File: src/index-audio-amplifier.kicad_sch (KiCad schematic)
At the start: 61 parts, among them J1 CU3616SASCLA004-LF, J2 SWD_PicoprobeCandybar, J3 Conn_01x02, J4 Conn_01x02, U1 RP2040, U2 RT6150B-33GQW, U3 W25Q16JVUXIQ, U4 MAX98360CENL, U5 TLV70033_SOT23-5, U6 MAX98360CENL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

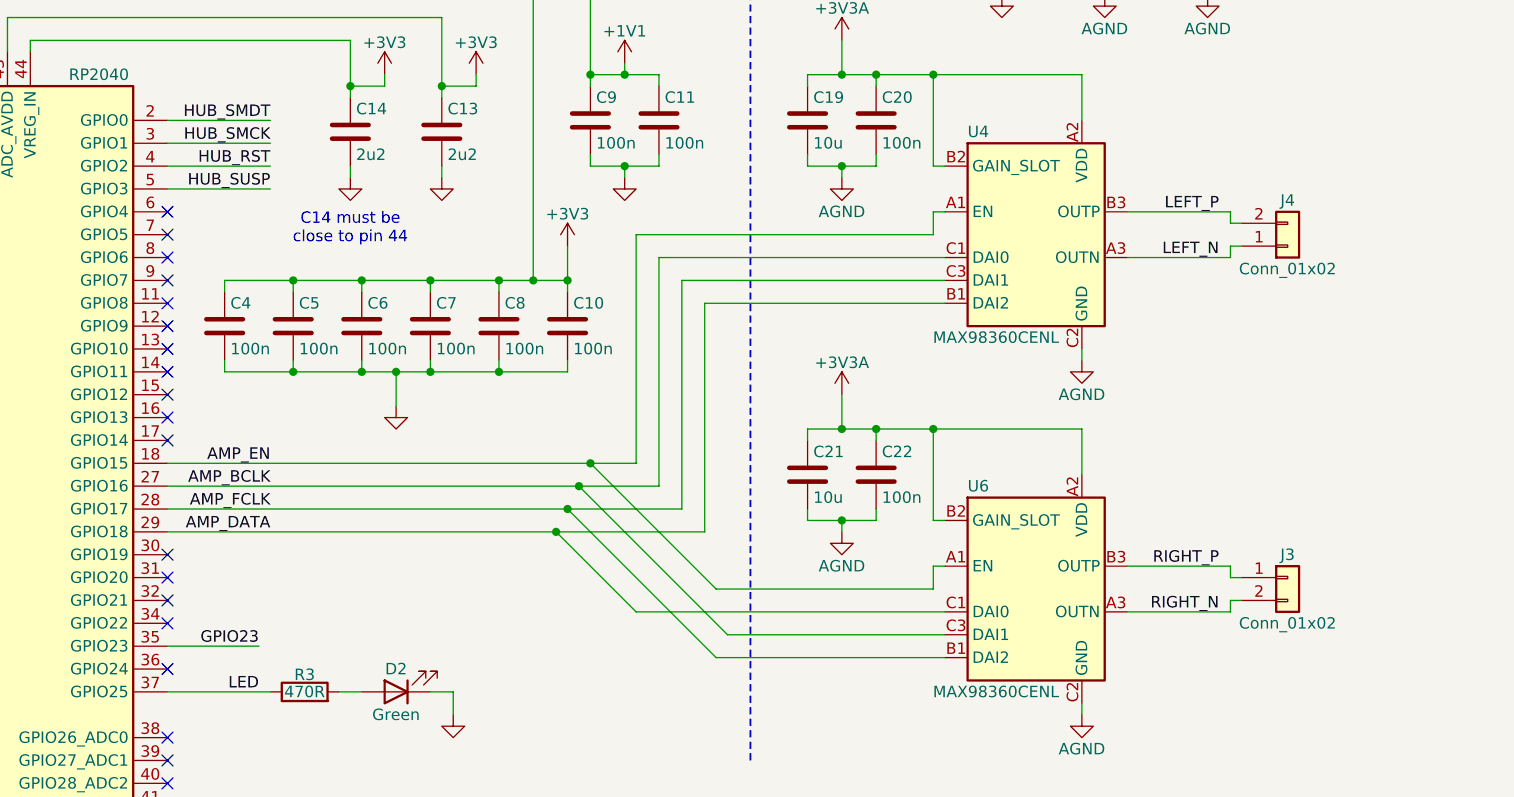
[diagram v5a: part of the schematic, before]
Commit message: Tie MAX98360 ENs to VDD to save on traces
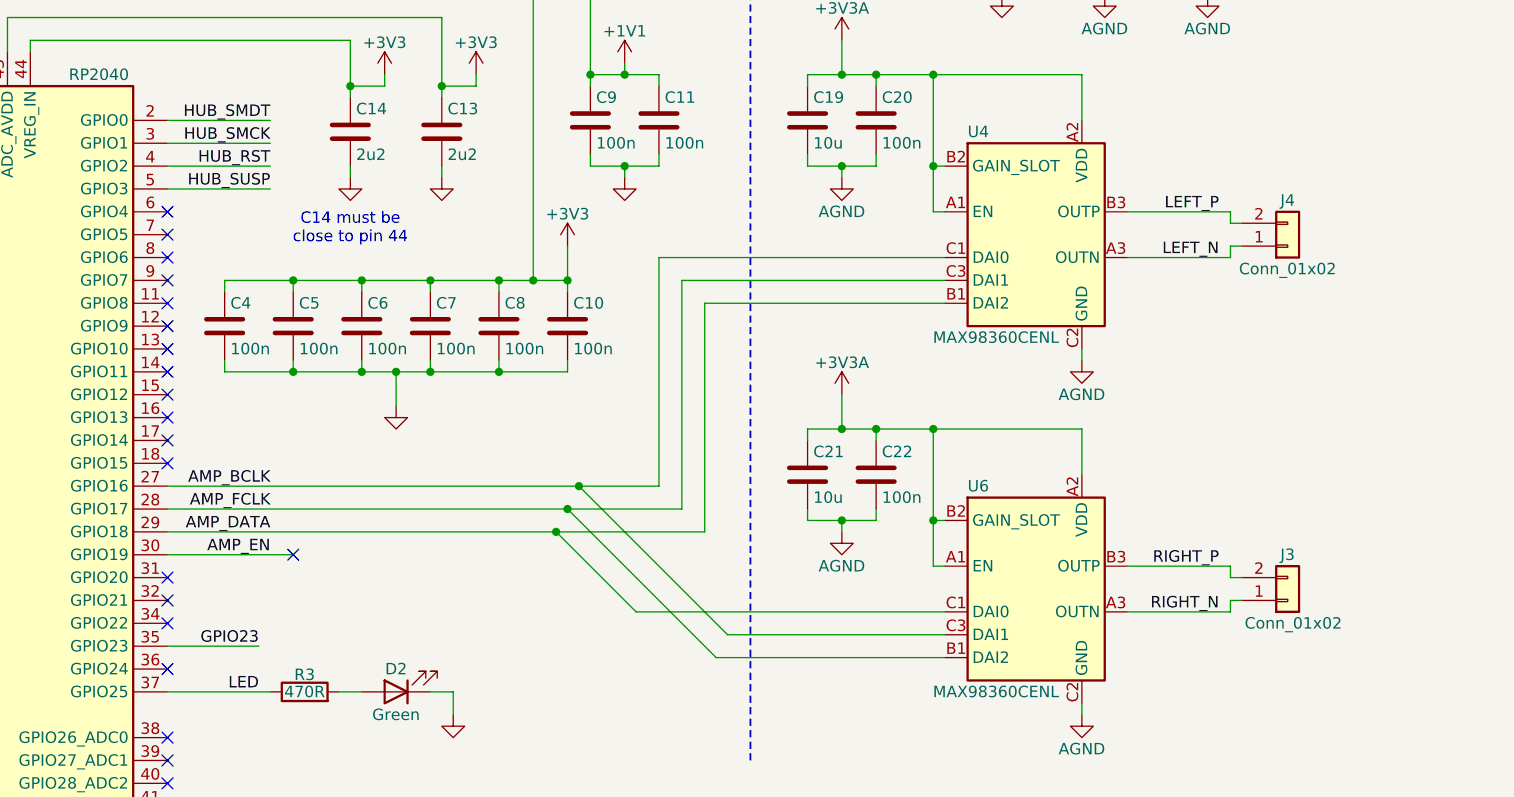
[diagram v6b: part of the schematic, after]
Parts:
- C19, C21: footprint Capacitor_SMD:C_0603_1608Metric -> Capacitor_SMD:C_0402_1005Metric
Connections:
- net +3V3A: now also U4.A1 (EN), U6.A1 (EN)
- net AMP_EN: now also U1.30 (GPIO19); no longer U1.18 (GPIO15), U4.A1 (EN), U6.A1 (EN)
- net RIGHT_N: now also J3.1 (Pin_1); no longer J3.2 (Pin_2)
- net RIGHT_P: now also J3.2 (Pin_2); no longer J3.1 (Pin_1)
- no-connect marks 31 -> 32
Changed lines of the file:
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@@
 	)
 	(junction
+		(at 236.22 151.13)
+		(diameter 0)
+		(color 0 0 0 0)
+	)
+	(junction
 		(at 35.56 90.17)
 		(diameter 0)
@@
 	)
 	(junction
-		(at 198.12 144.78)
-		(diameter 0)
-		(color 0 0 0 0)
-	)
-	(junction
 		(at 72.39 39.37)
 		(diameter 0)
@@
 	)
 	(junction
+		(at 236.22 111.76)
+		(diameter 0)
+		(color 0 0 0 0)
+	)
+	(junction
 		(at 97.79 25.4)
 		(diameter 0)
@@
 	)
 	(no_connect
+		(at 165.1 154.94)
+	)
+	(no_connect
 		(at 151.13 162.56)
 	)
@@
 	)
 	(no_connect
-		(at 151.13 154.94)
+		(at 151.13 144.78)
 	)
 	(no_connect
@@
 	(wire
 		(pts
-			(xy 203.2 119.38) (xy 236.22 119.38)
-		)
-		(stroke
-			(width 0)
-			(type default)
-		)
-	)
-	(wire
-		(pts
 			(xy 171.45 97.79) (xy 171.45 102.87)
 		)
@@
 	(wire
 		(pts
+			(xy 236.22 111.76) (xy 236.22 116.84)
+		)
+		(stroke
+			(width 0)
+			(type default)
+		)
+	)
+	(wire
+		(pts
 			(xy 107.95 25.4) (xy 97.79 25.4)
 		)
@@
 	(wire
 		(pts
-			(xy 236.22 158.75) (xy 236.22 156.21)
-		)
-		(stroke
-			(width 0)
-			(type default)
-		)
-	)
-	(wire
-		(pts
 			(xy 269.24 157.48) (xy 270.51 157.48)
 		)
@@
 	(wire
 		(pts
-			(xy 198.12 144.78) (xy 212.09 158.75)
-		)
-		(stroke
-			(width 0)
-			(type default)
-		)
-	)
-	(wire
-		(pts
 			(xy 44.45 25.4) (xy 55.88 25.4)
 		)
@@
 	(wire
 		(pts
-			(xy 151.13 144.78) (xy 198.12 144.78)
-		)
-		(stroke
-			(width 0)
-			(type default)
-		)
-	)
-	(wire
-		(pts
 			(xy 201.93 100.33) (xy 201.93 101.6)
 		)
@@
 	(wire
 		(pts
-			(xy 212.09 158.75) (xy 236.22 158.75)
+			(xy 111.76 48.26) (xy 111.76 49.53)
 		)
 		(stroke
@@
 	(wire
 		(pts
-			(xy 111.76 48.26) (xy 111.76 49.53)
+			(xy 102.87 38.1) (xy 111.76 38.1)
 		)
 		(stroke
@@
 	(wire
 		(pts
-			(xy 102.87 38.1) (xy 111.76 38.1)
+			(xy 184.15 45.72) (xy 185.42 45.72)
 		)
 		(stroke
@@
 	(wire
 		(pts
-			(xy 184.15 45.72) (xy 185.42 45.72)
+			(xy 135.89 97.79) (xy 171.45 97.79)
 		)
 		(stroke
@@
 	(wire
 		(pts
-			(xy 135.89 97.79) (xy 171.45 97.79)
+			(xy 49.53 118.11) (xy 57.15 118.11)
 		)
 		(stroke
@@
 	(wire
 		(pts
-			(xy 49.53 118.11) (xy 57.15 118.11)
+			(xy 119.38 34.29) (xy 118.11 34.29)
 		)
 		(stroke
@@
 	(wire
 		(pts
-			(xy 119.38 34.29) (xy 118.11 34.29)
+			(xy 60.96 63.5) (xy 60.96 39.37)
 		)
 		(stroke
@@
 	(wire
 		(pts
-			(xy 60.96 63.5) (xy 60.96 39.37)
+			(xy 151.13 154.94) (xy 165.1 154.94)
 		)
 		(stroke
@@
 	(wire
 		(pts
-			(xy 236.22 119.38) (xy 236.22 116.84)
-		)
-		(stroke
-			(width 0)
-			(type default)
-		)
-	)
-	(wire
-		(pts
 			(xy 72.39 36.83) (xy 72.39 39.37)
 		)
@@
 	(wire
 		(pts
-			(xy 198.12 144.78) (xy 203.2 144.78)
-		)
-		(stroke
-			(width 0)
-			(type default)
-		)
-	)
-	(wire
-		(pts
 			(xy 40.64 66.04) (xy 40.64 69.85)
 		)
@@
 	(wire
 		(pts
-			(xy 203.2 119.38) (xy 203.2 144.78)
+			(xy 236.22 151.13) (xy 236.22 156.21)
 		)
 		(stroke
@@
 	)
 	(label "AMP_EN"
-		(at 162.56 144.78 180)
+		(at 162.56 154.94 180)
 		(effects
 			(font
@@
 	(symbol
 		(lib_id "Connector_Generic:Conn_01x02")
-		(at 275.59 157.48 0)
+		(at 275.59 160.02 0)
+		(mirror x)
 		(unit 1)
 		(exclude_from_sim no)
@@
 		)
 		(property "Value" "Conn_01x02"
-			(at 275.59 162.56 0)
+			(at 276.225 162.56 0)
 			(effects
 				(font
@@
 		)
 		(property "Footprint" "Connector_PinHeader_1.00mm:PinHeader_1x02_P1.00mm_Vertical"
-			(at 275.59 157.48 0)
+			(at 275.59 160.02 0)
 			(effects
 				(font
@@
 		)
 		(property "Datasheet" "~"
-			(at 275.59 157.48 0)
+			(at 275.59 160.02 0)
 			(effects
 				(font
@@
 		)
 		(property "Description" "Generic connector, single row, 01x02, script generated (kicad-library-utils/schlib/autogen/connector/)"
-			(at 275.59 157.48 0)
+			(at 275.59 160.02 0)
 			(effects
 				(font
@@
 			)
 		)
-		(property "Footprint" "Capacitor_SMD:C_0603_1608Metric"
+		(property "Footprint" "Capacitor_SMD:C_0402_1005Metric"
 			(at 223.2152 110.49 0)
 			(effects
@@
 			)
 		)
-		(property "Footprint" "Capacitor_SMD:C_0603_1608Metric"
+		(property "Footprint" "Capacitor_SMD:C_0402_1005Metric"
 			(at 223.2152 149.86 0)
 			(effects

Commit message: Remove VBUS diode to save space (be careful!)
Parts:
- removed D1: MBR120VLSFT1G, Diode_SMD:D_SOD-123F, symbol Diode:MBR1020VL
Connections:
- net VSYS is gone; now on net VBUS: C1.1, C101.1, J2.4 (VCC), U2.5 (VIN), U2.6 (EN), U2.8 (VINA), U5.1 (IN), U5.3 (EN)
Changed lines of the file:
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@@
 	(wire
 		(pts
-			(xy 72.39 25.4) (xy 81.28 25.4)
+			(xy 72.39 25.4) (xy 97.79 25.4)
 		)
 		(stroke
@@
 	(wire
 		(pts
-			(xy 88.9 25.4) (xy 97.79 25.4)
-		)
-		(stroke
-			(width 0)
-			(type default)
-		)
-	)
-	(wire
-		(pts
 			(xy 201.93 111.76) (xy 205.74 111.76)
 		)
@@
 					(unit 1)
 				)
-			)
-		)
-	)
-	(symbol
-		(lib_id "Diode:MBR1020VL")
-		(at 85.09 25.4 180)
-		(unit 1)
-		(exclude_from_sim no)
-		(in_bom yes)
-		(on_board yes)
-		(dnp no)
-		(property "Reference" "D1"
-			(at 85.09 27.94 0)
-			(effects
-				(font
-					(size 1.27 1.27)
-				)
-			)
-		)
-		(property "Value" "MBR120VLSFT1G"
-			(at 85.09 22.86 0)
-			(effects
-				(font
-					(size 1.27 1.27)
-				)
-			)
-		)
-		(property "Footprint" "Diode_SMD:D_SOD-123F"
-			(at 85.09 20.955 0)
-			(effects
-				(font
-					(size 1.27 1.27)
-				)
-				(hide yes)
-			)
-		)
-		(property "Datasheet" "https://www.onsemi.com/download/data-sheet/pdf/mbr120vlsft1-d.pdf"
-			(at 85.09 25.4 0)
-			(effects
-				(font
-					(size 1.27 1.27)
-				)
-				(hide yes)
-			)
-		)
-		(property "Description" "Schottky Diode Rectifier, SOD-123F"
-			(at 85.09 25.4 0)
-			(effects
-				(font
-					(size 1.27 1.27)
-				)
-				(hide yes)
-			)
-		)
-		(pin "1"
-		)
-		(pin "2"
-		)
-		(instances
-			(project "index-audio-amplifier"
-				(path "/dc35f43b-99fc-498e-a143-7e0669c7658b"
-					(reference "D1")
-					(unit 1)
-				)

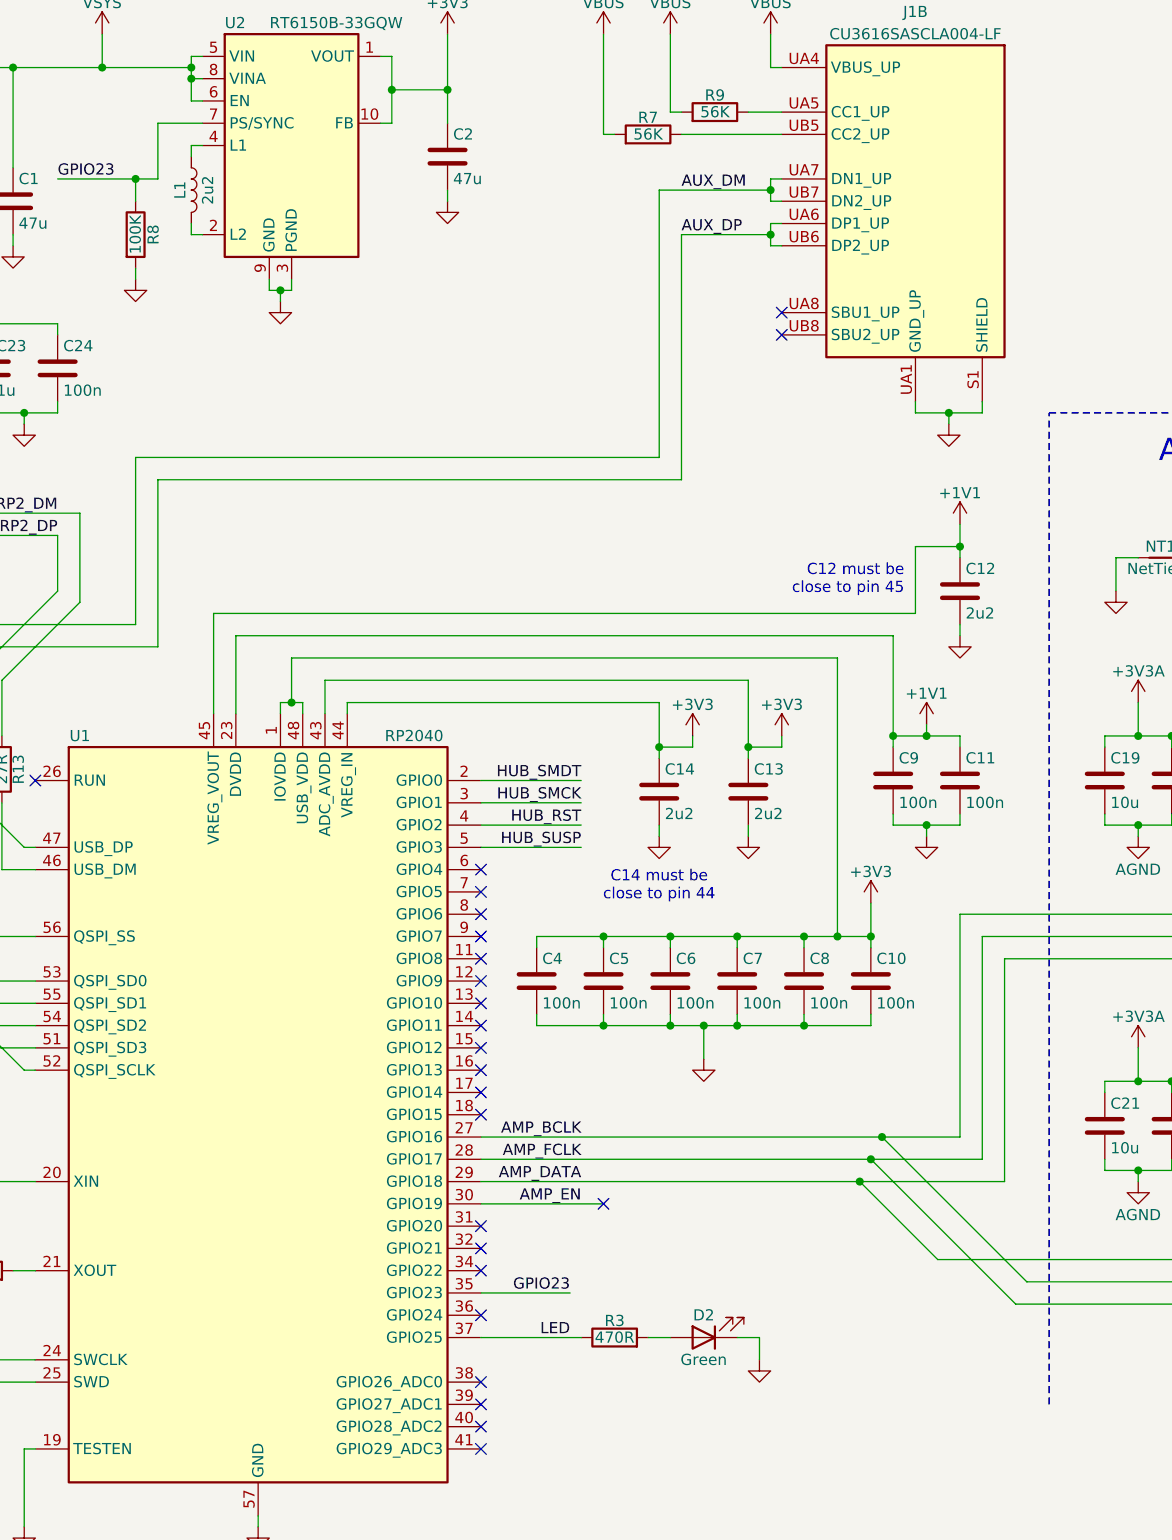
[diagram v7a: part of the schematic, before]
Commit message: Move LED to GPIO14 to support layout
(also make LED blue)
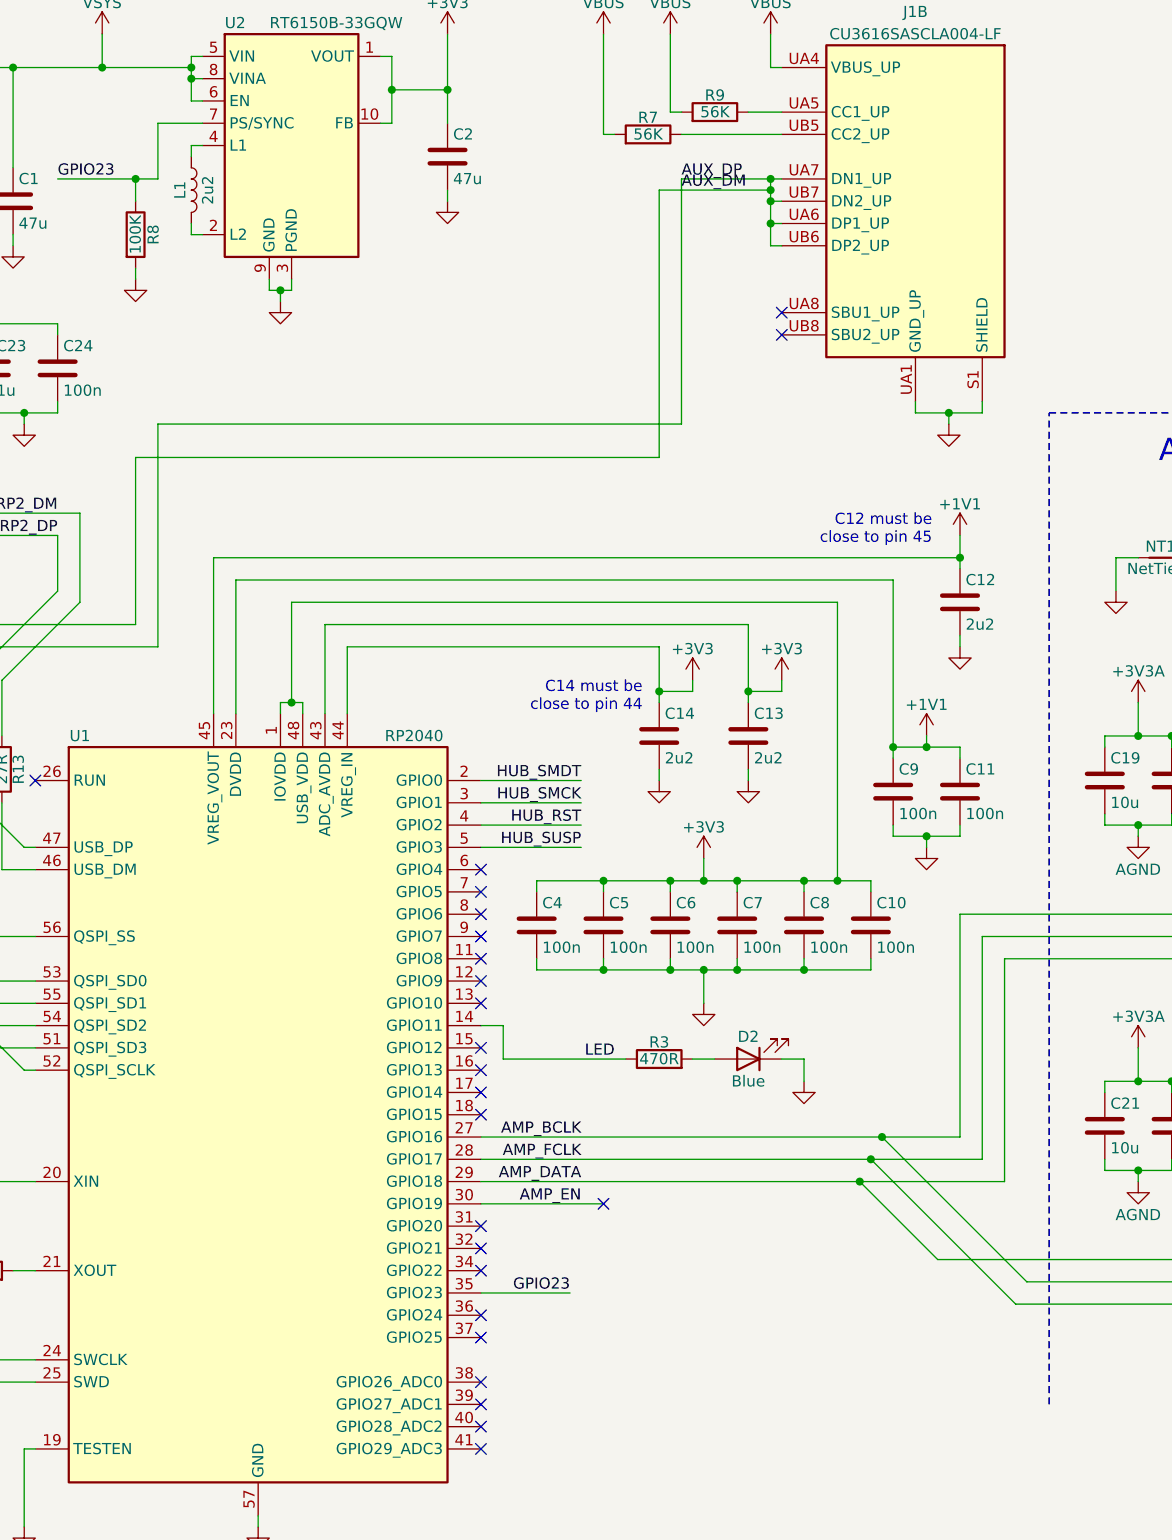
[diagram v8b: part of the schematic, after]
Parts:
- D2: value Green -> Blue
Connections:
- net AUX_DP is gone; now on net AUX_DM: J1.UA6 (DP1_UP), J1.UB6 (DP2_UP), U7.5 (USBDP_DN2)
- net LED: now also U1.14 (GPIO11); no longer U1.37 (GPIO25)
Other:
- moved on the sheet: C10, C11, C12, C13, C14, C4, C5, C6, C7, C8, C9, D2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
